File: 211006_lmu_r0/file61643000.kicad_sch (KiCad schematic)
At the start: 8 parts, among them J10 Conn_01x02, J8 Conn_01x02, J9 Conn_01x02, K1 G5V-2, Q38 BC817

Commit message: Updated lmu project with relative library paths and fixed broken symbols
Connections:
- net GND: now reaches Q38.2 (E)
- net GND: now also K1.6, R205.1
- net +3V3: now reaches K1.1
- net +3V3: now also K1.8
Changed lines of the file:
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@@
       (effects (font (size 1.27 1.27)) hide)
     )
+    (pin "1")
   )
   (symbol (lib_id "gnd_iso:GND_ISO") (at 151.13 118.11 0) (unit 1)
@@
       (effects (font (size 1.27 1.27)) hide)
     )
+    (pin "1")
   )
   (symbol (lib_id "gnd_iso:GND_ISO") (at 173.99 118.11 0) (unit 1)
@@
       (effects (font (size 1.27 1.27)) hide)
     )
+    (pin "1")
   )
   (symbol (lib_id "Device:R") (at 167.64 93.98 270) (unit 1)
@@
       (effects (font (size 1.27 1.27)) hide)
     )
+    (pin "1")
   )
   (symbol (lib_id "+3v3_iso:+3V3_ISO") (at 151.13 71.12 0) (unit 1)
@@
       (effects (font (size 1.27 1.27)) hide)
     )
+    (pin "1")
   )
   (symbol (lib_id "Connector_Generic:Conn_01x02") (at 101.6 63.5 180) (unit 1)

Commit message: Updated some components to make sourcing easier
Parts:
- J10, J8, J9, R203, R204, R205: Manufacturer (none) -> -; Part Number (none) -> -
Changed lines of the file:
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@@
+      (effects (font (size 1.27 1.27)) hide)
+    )
+    (property "Part Number" "-" (id 4) (at 167.64 106.68 0)
+      (effects (font (size 1.27 1.27)) hide)
+    )
+    (property "Manufacturer" "-" (id 5) (at 167.64 106.68 0)
       (effects (font (size 1.27 1.27)) hide)
     )
@@
     )
     (property "Datasheet" "~" (id 3) (at 173.99 111.76 0)
+      (effects (font (size 1.27 1.27)) hide)
+    )
+    (property "Part Number" "-" (id 4) (at 173.99 111.76 0)
+      (effects (font (size 1.27 1.27)) hide)
+    )
+    (property "Manufacturer" "-" (id 5) (at 173.99 111.76 0)
       (effects (font (size 1.27 1.27)) hide)
     )
@@
       (effects (font (size 1.27 1.27)) hide)
     )
+    (property "Part Number" "-" (id 4) (at 118.11 63.5 0)
+      (effects (font (size 1.27 1.27)) hide)
+    )
+    (property "Manufacturer" "-" (id 5) (at 118.11 63.5 0)
+      (effects (font (size 1.27 1.27)) hide)
+    )
     (pin "1")
     (pin "2")
@@
       (effects (font (size 1.27 1.27)) hide)
     )
+    (property "Part Number" "-" (id 4) (at 167.64 93.98 0)
+      (effects (font (size 1.27 1.27)) hide)
+    )
+    (property "Manufacturer" "-" (id 5) (at 167.64 93.98 0)
+      (effects (font (size 1.27 1.27)) hide)
+    )
     (pin "1")
     (pin "2")
@@
       (effects (font (size 1.27 1.27)) hide)
     )
+    (property "Part Number" "-" (id 4) (at 101.6 63.5 0)
+      (effects (font (size 1.27 1.27)) hide)
+    )
+    (property "Manufacturer" "-" (id 5) (at 101.6 63.5 0)
+      (effects (font (size 1.27 1.27)) hide)
+    )
     (pin "1")
     (pin "2")
@@
       (effects (font (size 1.27 1.27)) hide)
     )
+    (property "Part Number" "-" (id 4) (at 101.6 81.28 0)
+      (effects (font (size 1.27 1.27)) hide)
+    )
+    (property "Manufacturer" "-" (id 5) (at 101.6 81.28 0)
+      (effects (font (size 1.27 1.27)) hide)
+    )

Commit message: fixed footprints for headers, started planning out zones
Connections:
- net +3V3 renamed +3V3_ISO
- net GND renamed GND_ISO
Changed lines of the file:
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@@
     (pin "1")
   )
-  (symbol (lib_id "gnd_iso:GND_ISO") (at 173.99 118.11 0) (unit 1)
+  (symbol (lib_name "GND_ISO_1") (lib_id "gnd_iso:GND_ISO") (at 173.99 118.11 0) (unit 1)
     (in_bom yes) (on_board yes)
     (property "Reference" "#PWR070" (id 0) (at 173.99 124.46 0)
@@
     (pin "2")
   )
-  (symbol (lib_id "gnd_iso:GND_ISO") (at 148.59 55.88 0) (unit 1)
+  (symbol (lib_name "GND_ISO_2") (lib_id "gnd_iso:GND_ISO") (at 148.59 55.88 0) (unit 1)
     (in_bom yes) (on_board yes)
     (property "Reference" "#PWR067" (id 0) (at 148.59 62.23 0)
@@
     (pin "1")
   )
-  (symbol (lib_id "+3v3_iso:+3V3_ISO") (at 151.13 71.12 0) (unit 1)
+  (symbol (lib_name "+3V3_ISO_1") (lib_id "+3v3_iso:+3V3_ISO") (at 151.13 71.12 0) (unit 1)
     (in_bom yes) (on_board yes)
     (property "Reference" "#PWR068" (id 0) (at 151.13 74.93 0)

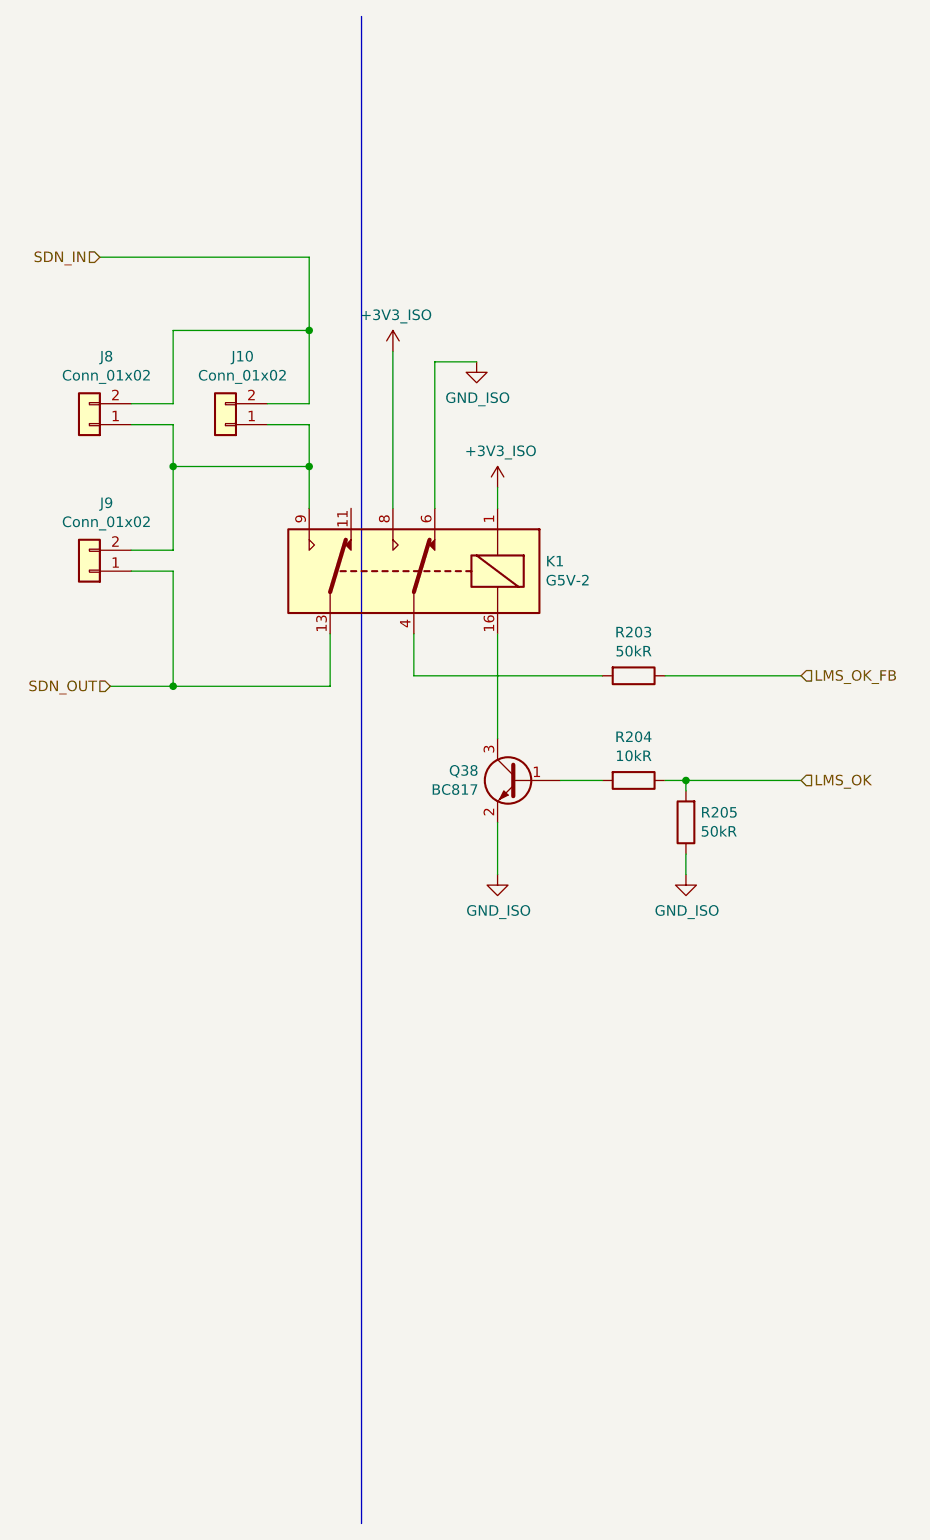
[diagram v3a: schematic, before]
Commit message: refined in-out routing mechanism
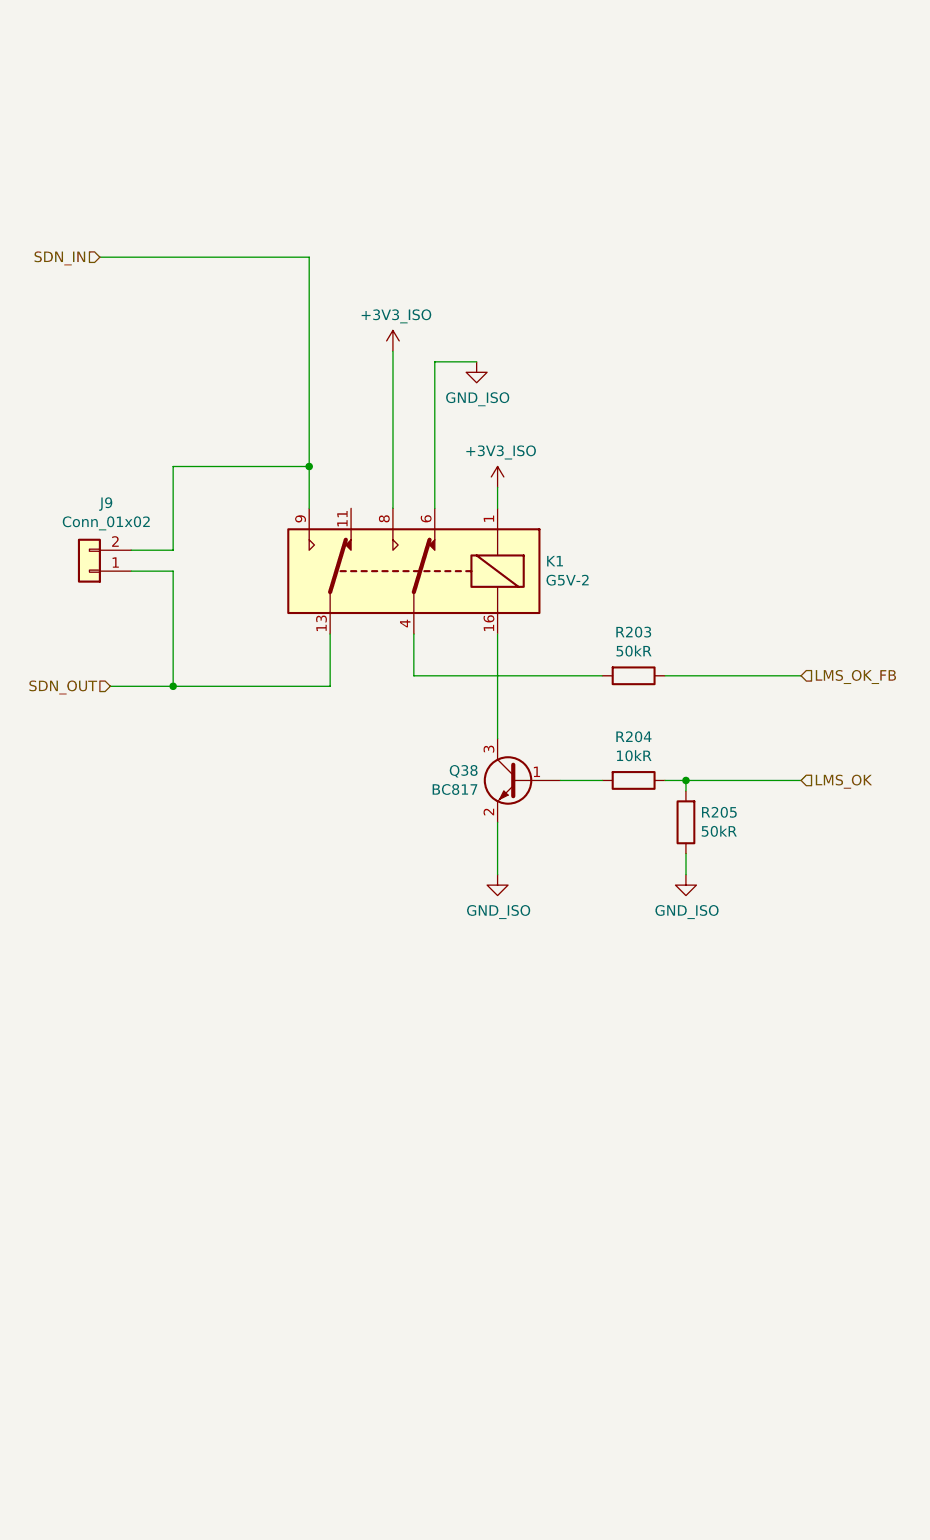
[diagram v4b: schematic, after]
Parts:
- removed J10, J8: Conn_01x02, Connector_PinHeader_2.54mm:PinHeader_1x02_P2.54mm_Vertical, symbol Connector_Generic:Conn_01x02
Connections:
- net SDN_IN: now also J9.2 (Pin_2), K1.9
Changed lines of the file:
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@@
   (junction (at 128.27 68.58) (diameter 0) (color 0 0 0 0)
   )
-  (junction (at 128.27 52.07) (diameter 0) (color 0 0 0 0)
-  )
-  (junction (at 111.76 68.58) (diameter 0) (color 0 0 0 0)
-  )
   (junction (at 173.99 106.68) (diameter 0) (color 0 0 0 0)
   )
@@
     (stroke (width 0) (type default) (color 0 0 0 0))
   )
-  (wire (pts (xy 111.76 52.07) (xy 128.27 52.07))
-    (stroke (width 0) (type default) (color 0 0 0 0))
-  )
-  (wire (pts (xy 123.19 60.96) (xy 128.27 60.96))
-    (stroke (width 0) (type default) (color 0 0 0 0))
-  )
   (wire (pts (xy 173.99 106.68) (xy 173.99 107.95))
     (stroke (width 0) (type default) (color 0 0 0 0))
@@
     (stroke (width 0) (type default) (color 0 0 0 0))
   )
-  (wire (pts (xy 128.27 43.18) (xy 128.27 52.07))
-    (stroke (width 0) (type default) (color 0 0 0 0))
-  )
   (wire (pts (xy 111.76 95.25) (xy 130.81 95.25))
     (stroke (width 0) (type default) (color 0 0 0 0))
   )
-  (polyline (pts (xy 134.62 196.85) (xy 134.62 13.97))
-    (stroke (width 0) (type default) (color 0 0 0 0))
-  )
   (wire (pts (xy 102.87 43.18) (xy 128.27 43.18))
     (stroke (width 0) (type default) (color 0 0 0 0))
@@
     (stroke (width 0) (type default) (color 0 0 0 0))
   )
-  (wire (pts (xy 123.19 63.5) (xy 128.27 63.5))
-    (stroke (width 0) (type default) (color 0 0 0 0))
-  )
   (wire (pts (xy 163.83 106.68) (xy 158.75 106.68))
     (stroke (width 0) (type default) (color 0 0 0 0))
@@
     (stroke (width 0) (type default) (color 0 0 0 0))
   )
-  (wire (pts (xy 111.76 60.96) (xy 111.76 52.07))
-    (stroke (width 0) (type default) (color 0 0 0 0))
-  )
-  (wire (pts (xy 128.27 63.5) (xy 128.27 68.58))
-    (stroke (width 0) (type default) (color 0 0 0 0))
-  )
   (wire (pts (xy 151.13 111.76) (xy 151.13 118.11))
     (stroke (width 0) (type default) (color 0 0 0 0))
@@
     (stroke (width 0) (type default) (color 0 0 0 0))
   )
-  (wire (pts (xy 106.68 60.96) (xy 111.76 60.96))
-    (stroke (width 0) (type default) (color 0 0 0 0))
-  )
   (wire (pts (xy 171.45 106.68) (xy 173.99 106.68))
     (stroke (width 0) (type default) (color 0 0 0 0))
   )
-  (wire (pts (xy 128.27 52.07) (xy 128.27 60.96))
+  (wire (pts (xy 128.27 43.18) (xy 128.27 68.58))
     (stroke (width 0) (type default) (color 0 0 0 0))
   )
@@
     (stroke (width 0) (type default) (color 0 0 0 0))
   )
-  (wire (pts (xy 106.68 63.5) (xy 111.76 63.5))
-    (stroke (width 0) (type default) (color 0 0 0 0))
-  )
   (wire (pts (xy 111.76 81.28) (xy 111.76 95.25))
-    (stroke (width 0) (type default) (color 0 0 0 0))
-  )
-  (wire (pts (xy 111.76 63.5) (xy 111.76 68.58))
     (stroke (width 0) (type default) (color 0 0 0 0))
   )
@@
     (pin "9")
   )
-  (symbol (lib_id "Connector_Generic:Conn_01x02") (at 118.11 63.5 180) (unit 1)
-    (in_bom yes) (on_board yes)
-    (property "Reference" "J10" (id 0) (at 120.1928 55.245 0))
-    (property "Value" "Conn_01x02" (id 1) (at 120.1928 57.5564 0))
-    (property "Footprint" "Connector_PinHeader_2.54mm:PinHeader_1x02_P2.54mm_Vertical" (id 2) (at 118.11 63.5 0)
-      (effects (font (size 1.27 1.27)) hide)
-    )
-    (property "Datasheet" "~" (id 3) (at 118.11 63.5 0)
-      (effects (font (size 1.27 1.27)) hide)
-    )
-    (property "Part Number" "-" (id 4) (at 118.11 63.5 0)
-      (effects (font (size 1.27 1.27)) hide)
-    )
-    (property "Manufacturer" "-" (id 5) (at 118.11 63.5 0)
-      (effects (font (size 1.27 1.27)) hide)
-    )
-    (pin "1")
-    (pin "2")
-  )
   (symbol (lib_id "+3v3_iso:+3V3_ISO") (at 138.43 54.61 0) (unit 1)
     (in_bom yes) (on_board yes)
@@
     (pin "1")
   )
-  (symbol (lib_id "Connector_Generic:Conn_01x02") (at 101.6 63.5 180) (unit 1)
-    (in_bom yes) (on_board yes)
-    (property "Reference" "J8" (id 0) (at 103.6828 55.245 0))
-    (property "Value" "Conn_01x02" (id 1) (at 103.6828 57.5564 0))
-    (property "Footprint" "Connector_PinHeader_2.54mm:PinHeader_1x02_P2.54mm_Vertical" (id 2) (at 101.6 63.5 0)
-      (effects (font (size 1.27 1.27)) hide)
-    )
-    (property "Datasheet" "~" (id 3) (at 101.6 63.5 0)
-      (effects (font (size 1.27 1.27)) hide)
-    )
-    (property "Part Number" "-" (id 4) (at 101.6 63.5 0)
-      (effects (font (size 1.27 1.27)) hide)
-    )
-    (property "Manufacturer" "-" (id 5) (at 101.6 63.5 0)
-      (effects (font (size 1.27 1.27)) hide)
-    )
-    (pin "1")
-    (pin "2")
-  )
   (symbol (lib_id "Connector_Generic:Conn_01x02") (at 101.6 81.28 180) (unit 1)

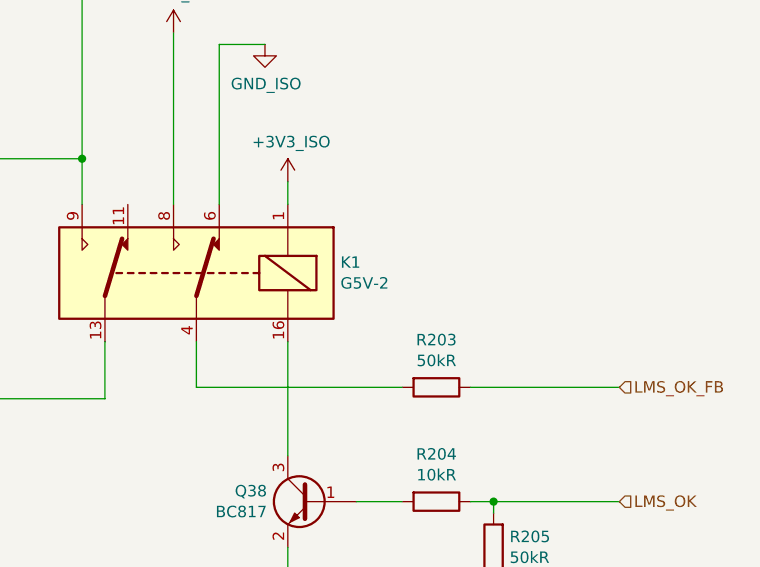
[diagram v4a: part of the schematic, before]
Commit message: sorted header location
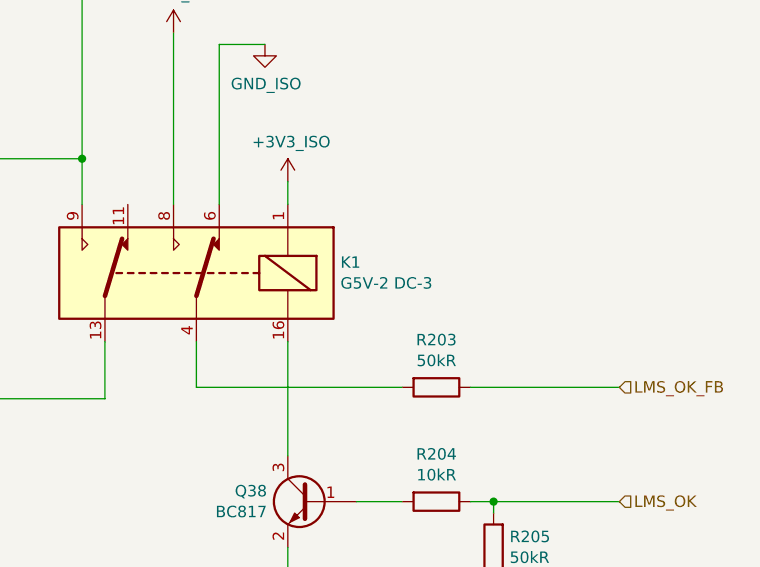
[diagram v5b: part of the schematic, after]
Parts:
- K1: value G5V-2 -> G5V-2 DC-3; Mouser Part Number 653-G5V-2-H1-DC12 -> 653-G5V-2-H1DC3; Part Number G5V-2-H1-DC12 -> G5V-2-H1 DC3
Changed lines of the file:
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@@
       (effects (font (size 1.27 1.27)) (justify right))
     )
-    (property "Value" "G5V-2" (id 1) (at 156.972 82.423 0)
+    (property "Value" "G5V-2 DC-3" (id 1) (at 156.972 82.423 0)
       (effects (font (size 1.27 1.27)) (justify right))
     )
@@
       (effects (font (size 1.27 1.27)) hide)
     )
-    (property "Mouser Part Number" "653-G5V-2-H1-DC12" (id 5) (at 140.97 81.28 0)
+    (property "Mouser Part Number" "653-G5V-2-H1DC3" (id 5) (at 140.97 81.28 0)
       (effects (font (size 1.27 1.27)) hide)
     )
@@
       (effects (font (size 1.27 1.27)) hide)
     )
-    (property "Part Number" "G5V-2-H1-DC12" (id 7) (at 140.97 81.28 0)
+    (property "Part Number" "G5V-2-H1 DC3" (id 7) (at 140.97 81.28 0)
       (effects (font (size 1.27 1.27)) hide)
     )
